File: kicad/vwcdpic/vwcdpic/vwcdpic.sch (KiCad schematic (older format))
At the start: 11 parts, among them U1 PIC12F629, U2 LM78L05ACZ

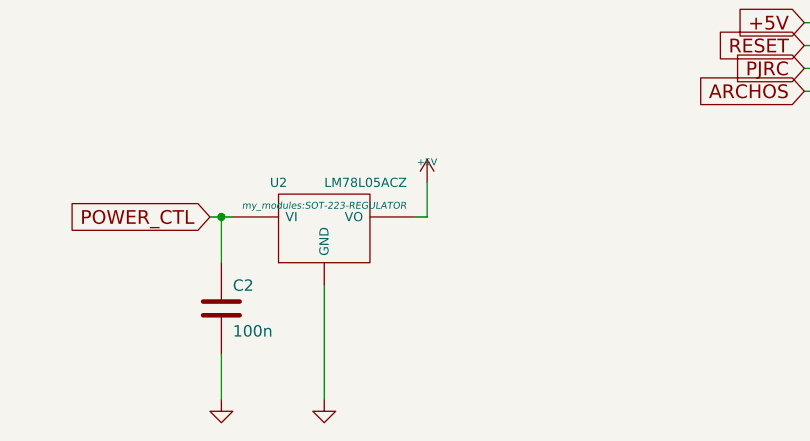
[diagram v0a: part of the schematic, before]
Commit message: 78L05 int SOT23 package as alternative to AM1117
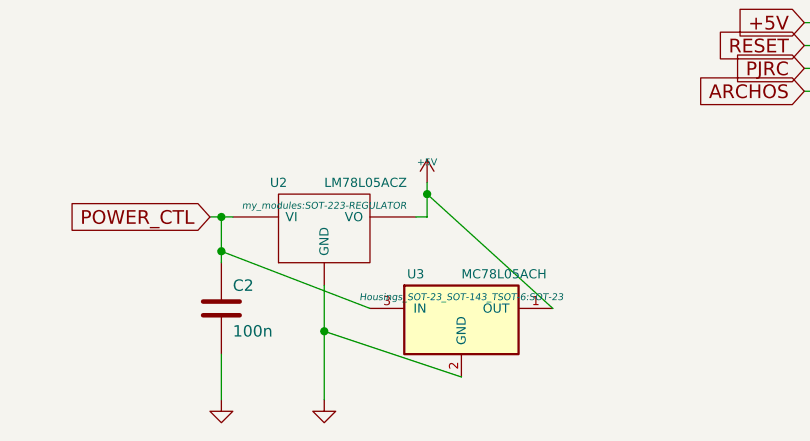
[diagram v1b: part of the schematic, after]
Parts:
- added U3: MC78L05ACH, Housings_SOT-23_SOT-143_TSOT-6:SOT-23, symbol MC78L05ACH
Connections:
- net +5V: now also U3.1 (OUT)
- net GND: now also U3.2 (GND)
- net POWER_CTL: now also U3.3 (IN)
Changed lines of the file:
@@
 EESchema Schematic File Version 2
-LIBS:emulator-rescue
 LIBS:power
 LIBS:device
@@
 LIBS:phonejack
 LIBS:device_sot
-LIBS:emulator-cache
+LIBS:vwcdpic-rescue
+LIBS:vwcdpic-cache
 EELAYER 25 0
 EELAYER END
@@
 POWER_CTL
 $Comp
-L GND #PWR01
+L GND #PWR7
 U 1 1 52D3D3F9
 P 6900 3550
-F 0 "#PWR01" H 6900 3550 30  0001 C CNN
+F 0 "#PWR7" H 6900 3550 30  0001 C CNN
 F 1 "GND" H 6900 3480 30  0001 C CNN
 F 2 "" H 6900 3550 60  0001 C CNN
@@
 DataIn-PRG_CLK
 $Comp
-L +5V #PWR02
+L +5V #PWR2
 U 1 1 52D03030
 P 3400 2350
-F 0 "#PWR02" H 3400 2440 20  0001 C CNN
+F 0 "#PWR2" H 3400 2440 20  0001 C CNN
 F 1 "+5V" H 3400 2440 30  0000 C CNN
 F 2 "" H 3400 2350 60  0001 C CNN
@@
 $EndComp
 $Comp
-L +5V #PWR03
+L +5V #PWR6
 U 1 1 52D02FCA
 P 5950 5000
-F 0 "#PWR03" H 5950 5090 20  0001 C CNN
+F 0 "#PWR6" H 5950 5090 20  0001 C CNN
 F 1 "+5V" H 5950 5090 30  0000 C CNN
 F 2 "" H 5950 5000 60  0001 C CNN
@@
 $EndComp
 $Comp
-L GND #PWR04
+L GND #PWR3
 U 1 1 52D02FB7
 P 4850 3050
-F 0 "#PWR04" H 4850 3050 30  0001 C CNN
+F 0 "#PWR3" H 4850 3050 30  0001 C CNN
 F 1 "GND" H 4850 2980 30  0001 C CNN
 F 2 "" H 4850 3050 60  0001 C CNN
@@
 $EndComp
 $Comp
-L GND #PWR05
+L GND #PWR5
 U 1 1 52D02FA3
 P 5500 5950
-F 0 "#PWR05" H 5500 5950 30  0001 C CNN
+F 0 "#PWR5" H 5500 5950 30  0001 C CNN
 F 1 "GND" H 5500 5880 30  0001 C CNN
 F 2 "" H 5500 5950 60  0001 C CNN
@@
 $EndComp
 $Comp
-L GND #PWR06
+L GND #PWR4
 U 1 1 52D02FA1
 P 5050 5950
-F 0 "#PWR06" H 5050 5950 30  0001 C CNN
+F 0 "#PWR4" H 5050 5950 30  0001 C CNN
 F 1 "GND" H 5050 5880 30  0001 C CNN
 F 2 "" H 5050 5950 60  0001 C CNN
@@
 	1    0    0    -1
 $EndComp
-Wire Wire Line
-	5050 5350 5050 5150
-Wire Wire Line
-	3150 3950 3400 3950
-Connection ~ 3400 2500
-Connection ~ 5050 5150
-Wire Wire Line
-	5900 5150 5950 5150
-Wire Wire Line
-	6900 3500 7700 3500
-Wire Wire Line
-	7650 3600 7700 3600
-Wire Wire Line
-	7650 3800 7700 3800
-Wire Wire Line
-	5550 3950 5750 3950
-Wire Wire Line
-	5550 3650 5750 3650
-Wire Wire Line
-	5050 5750 5050 5950
-Wire Wire Line
-	5050 3250 4850 3250
-Wire Wire Line
-	4850 3650 5050 3650
-Wire Wire Line
-	4850 3950 5050 3950
-Wire Wire Line
-	5550 3250 5750 3250
-Wire Wire Line
-	7650 3700 7700 3700
-Wire Wire Line
-	7650 3400 7700 3400
-Wire Wire Line
-	5500 5450 5500 5950
-Wire Wire Line
-	4300 2500 4850 2500
-Wire Wire Line
-	4850 2500 4850 3050
-Connection ~ 4850 2950
-Wire Wire Line
-	5000 5150 5100 5150
-Wire Wire Line
-	6900 3500 6900 3550
-Wire Wire Line
-	3400 2350 3400 2950
-Wire Wire Line
-	3150 2750 3150 2500
-Wire Wire Line
-	3150 3250 3150 4000
-Wire Wire Line
-	3400 3250 3400 3450
-Wire Wire Line
-	3400 3450 2850 3450
-Wire Wire Line
-	3400 3550 3400 3650
-Wire Wire Line
-	5950 5150 5950 5000
-Wire Wire Line
-	2850 3650 3150 3650
-Connection ~ 3150 3650
-Connection ~ 3150 2500
-Wire Wire Line
-	2950 2500 3900 2500
-Wire Wire Line
-	2950 2500 2950 3750
-Wire Wire Line
-	2950 3750 2850 3750
 $Comp
 L CP C1
@@
 $EndComp
 $Comp
-L GND #PWR07
+L GND #PWR1
 U 1 1 55C4B8F3
 P 3150 4400
-F 0 "#PWR07" H 3150 4400 30  0001 C CNN
+F 0 "#PWR1" H 3150 4400 30  0001 C CNN
 F 1 "GND" H 3150 4330 30  0001 C CNN
 F 2 "" H 3150 4400 60  0001 C CNN
@@
 	1    0    0    -1
 $EndComp
-Wire Wire Line
-	3150 4400 3150 4300
-Connection ~ 3150 3950
-Wire Wire Line
-	2850 3550 3400 3550
-Wire Wire Line
-	7700 4600 7600 4600
-Wire Wire Line
-	7600 4500 7700 4500
-Wire Wire Line
-	7600 4400 7700 4400
-Wire Wire Line
-	7600 4300 7700 4300
 Text GLabel 7600 4300 0    60   Input ~ 0
 +5V
@@
 Text GLabel 7600 4500 0    60   Input ~ 0
 PJRC
+$Comp
+L MC78L05ACH U3
+U 1 1 561664C4
+P 6100 5600
+F 0 "U3" H 5900 5800 40  0000 C CNN
+F 1 "MC78L05ACH" H 6100 5800 40  0000 L CNN
+F 2 "Housings_SOT-23_SOT-143_TSOT-6:SOT-23" H 6100 5700 30  0000 C CIN
+F 3 "" H 6100 5600 60  0000 C CNN
+	1    6100 5600
+	1    0    0    -1
+$EndComp
+Wire Wire Line
+	5050 5350 5050 5150
+Wire Wire Line
+	3150 3950 3400 3950
+Connection ~ 3400 2500
+Connection ~ 5050 5150
+Wire Wire Line
+	5900 5150 5950 5150
+Wire Wire Line
+	6900 3500 7700 3500
+Wire Wire Line
+	7650 3600 7700 3600
+Wire Wire Line
+	7650 3800 7700 3800
+Wire Wire Line
+	5550 3950 5750 3950
+Wire Wire Line
+	5550 3650 5750 3650
+Wire Wire Line
+	5050 5750 5050 5950
+Wire Wire Line
+	5050 3250 4850 3250
+Wire Wire Line
+	4850 3650 5050 3650
+Wire Wire Line
+	4850 3950 5050 3950
+Wire Wire Line
+	5550 3250 5750 3250
+Wire Wire Line
+	7650 3700 7700 3700
+Wire Wire Line
+	7650 3400 7700 3400
+Wire Wire Line
+	5500 5450 5500 5950
+Wire Wire Line
+	4300 2500 4850 2500
+Wire Wire Line
+	4850 2500 4850 3050
+Connection ~ 4850 2950
+Wire Wire Line
+	5000 5150 5100 5150
+Wire Wire Line
+	6900 3500 6900 3550
+Wire Wire Line
+	3400 2350 3400 2950
+Wire Wire Line
+	3150 2750 3150 2500
+Wire Wire Line
+	3150 3250 3150 4000
+Wire Wire Line
+	3400 3250 3400 3450
+Wire Wire Line
+	3400 3450 2850 3450
+Wire Wire Line
+	3400 3550 3400 3650
+Wire Wire Line
+	5950 5150 5950 5000
+Wire Wire Line
+	2850 3650 3150 3650
+Connection ~ 3150 3650
+Connection ~ 3150 2500
+Wire Wire Line
+	2950 2500 3900 2500
+Wire Wire Line
+	2950 2500 2950 3750
+Wire Wire Line
+	2950 3750 2850 3750
+Wire Wire Line
+	3150 4400 3150 4300
+Connection ~ 3150 3950
+Wire Wire Line
+	2850 3550 3400 3550
+Wire Wire Line
+	7700 4600 7600 4600
+Wire Wire Line
+	7600 4500 7700 4500
+Wire Wire Line
+	7600 4400 7700 4400
+Wire Wire Line
+	7600 4300 7700 4300
+Wire Wire Line
+	5700 5550 5050 5300
+Connection ~ 5050 5300
+Wire Wire Line
+	6100 5850 5500 5650
+Connection ~ 5500 5650
+Wire Wire Line
+	6500 5550 5950 5050
+Connection ~ 5950 5050
 $EndSCHEMATC
